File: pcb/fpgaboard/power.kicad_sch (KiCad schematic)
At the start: 77 parts, among them J1 Conn_02x02_Odd_Even, J2 USB_B_Micro, U1 LT3030EFE, U2 W25Q32JVSSIM, U3 ICE40HX8K-CT256, U4 93LC56B, U5 FT2232H, X1 12M

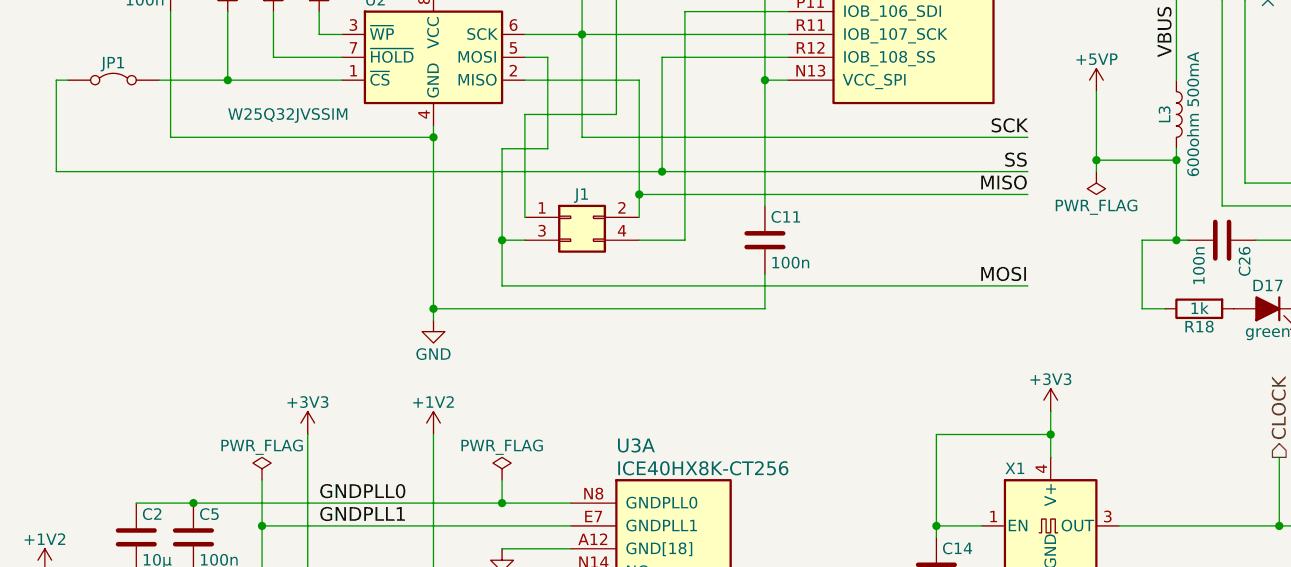
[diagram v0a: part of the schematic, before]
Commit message: Fix absolute paths and some labels
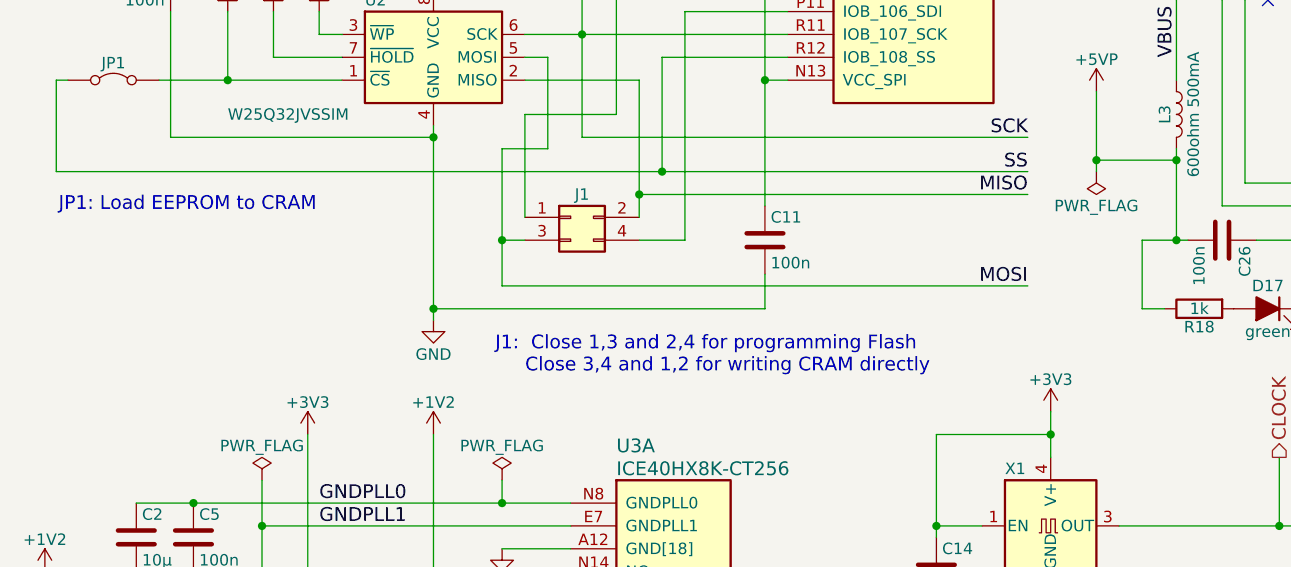
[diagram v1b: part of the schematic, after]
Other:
- note added: "J1: Close 1,3 and 2,4 for programming Flash Close 3,4 and 1,2 for writing CRAM directly"
- note added: "JP1: Load EEPROM to CRAM"
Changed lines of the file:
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@@
 	(title_block
 		(title "Game Boy reverse eng. FPGA board")
-		(date "2024-06-19")
+		(date "2024-12-09")
 		(rev "1")
 		(company "CC-BY-SA-4.0 Michael Singer")
@@
 		)
 	)
+	(text "JP1: Load EEPROM to CRAM"
+		(exclude_from_sim no)
+		(at 19.304 57.404 0)
+		(effects
+			(font
+				(size 1.524 1.524)
+			)
+			(justify left top)
+		)
+	)
+	(text "J1:  Close 1,3 and 2,4 for programming Flash\n     Close 3,4 and 1,2 for writing CRAM directly"
+		(exclude_from_sim no)
+		(at 67.818 72.898 0)
+		(effects
+			(font
+				(size 1.524 1.524)
+			)
+			(justify left top)
+		)
+	)
